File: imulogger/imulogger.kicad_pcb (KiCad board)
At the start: 2 copper layers, 64 x 25 mm, 23 parts, among them J1 DEBUG, J2 BATCONN, J3 CHGCONN, J4 Micro_SD_Card, SW1 SW_SPDT, U1 ESP32-WROOM-32, U2 USFS, U3 MCP1826S

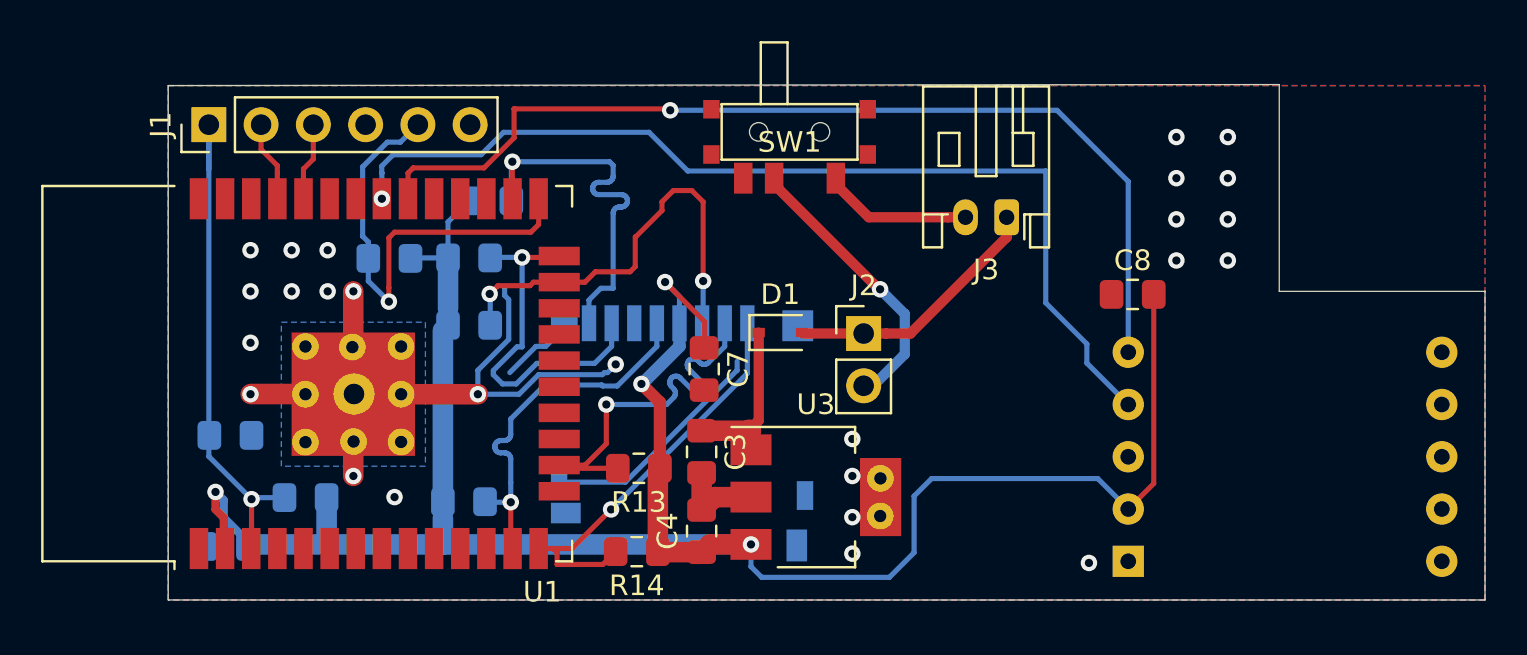
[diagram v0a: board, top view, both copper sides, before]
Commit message: make switch route V_BAT instead of GND
even though it shouldn't make a difference it's probably better to
not connect the system load to the charger.
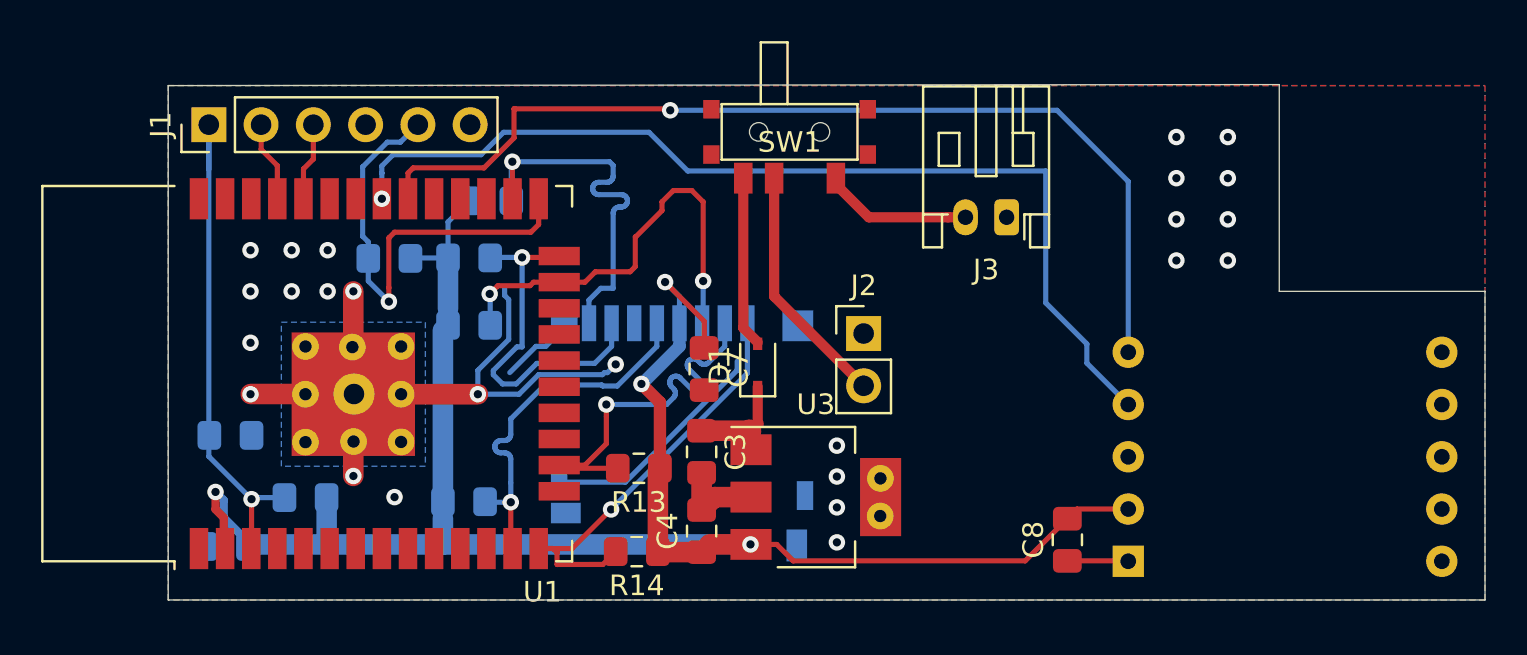
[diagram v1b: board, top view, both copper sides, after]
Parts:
- moved C8 12.3 mm to (163.7, 81.1), turned to 90 degrees
- moved D1 1.94 mm to (148.7, 72.6), turned to 90 degrees
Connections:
- J2 pad 1: Net-(D1-Pad2) -> GND
- J3 pad 1: Net-(D1-Pad2) -> GND
- SW1 pad 3: GND -> Net-(D1-Pad2)
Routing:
- net +3V3: track 110.4 -> 95.3 mm
- net Net-(D1-Pad2): track 12.9 -> 8.34 mm
- net GND: track 56.0 -> 59.0 mm, vias 26 -> 25
- net V_BAT: track 9.04 -> 6.45 mm
- net Net-(J2-Pad2): track 13.8 -> 12.7 mm, vias 1 -> 0

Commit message: optimize ground connection
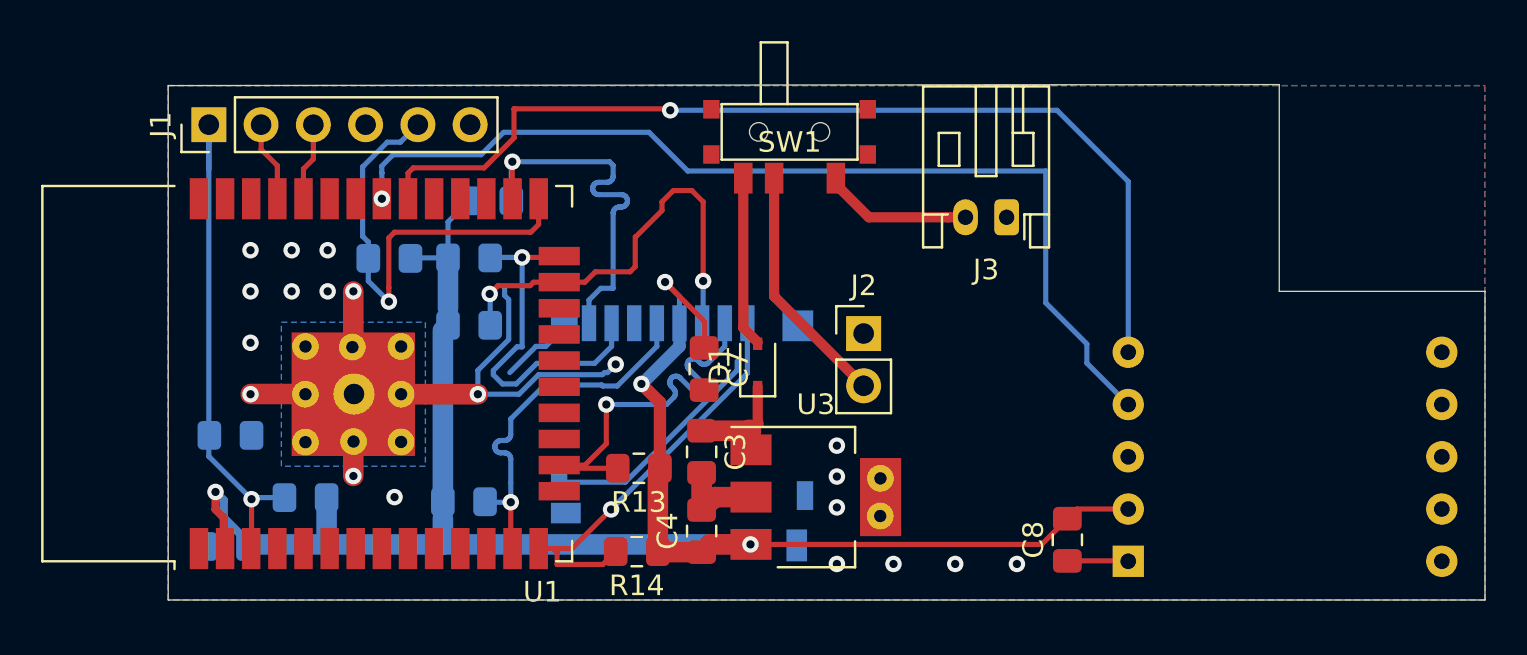
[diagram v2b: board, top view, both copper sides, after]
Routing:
- net +3V3: track 95.3 -> 94.7 mm
- net GND: vias 25 -> 20
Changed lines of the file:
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@@
     (thickness 1.6)
     (drawings 14)
-    (tracks 416)
+    (tracks 409)
     (zones 0)
     (modules 23)
@@
   (segment (start 164.17 79.58) (end 163.7 80.05) (width 0.25) (layer F.Cu) (net 1))
   (segment (start 166.66 79.58) (end 164.17 79.58) (width 0.25) (layer F.Cu) (net 1))
-  (segment (start 149.575 81.3) (end 150.375 82.1) (width 0.25) (layer F.Cu) (net 1))
-  (segment (start 148.325 81.3) (end 149.575 81.3) (width 0.25) (layer F.Cu) (net 1))
-  (segment (start 161.65 82.1) (end 163.7 80.05) (width 0.25) (layer F.Cu) (net 1))
-  (segment (start 150.375 82.1) (end 161.65 82.1) (width 0.25) (layer F.Cu) (net 1))
   (segment (start 148.3 81.3) (end 133.35 81.3) (width 1) (layer B.Cu) (net 1))
   (via (at 148.3 81.3) (size 0.8) (drill 0.4) (layers F.Cu B.Cu) (net 1))
-  (via (at 169 61.5) (size 0.8) (drill 0.4) (layers F.Cu B.Cu) (net 2))
-  (via (at 152.5 81.2) (size 0.8) (drill 0.4) (layers F.Cu B.Cu) (net 2))
+  (segment (start 162.45 81.3) (end 163.7 80.05) (width 0.25) (layer F.Cu) (net 1))
+  (segment (start 148.325 81.3) (end 162.45 81.3) (width 0.25) (layer F.Cu) (net 1))
+  (via (at 152.5 82.25) (size 0.8) (drill 0.4) (layers F.Cu B.Cu) (net 2))
   (via (at 152.5 79.5) (size 0.8) (drill 0.4) (layers F.Cu B.Cu) (net 2))
   (via (at 152.5 78) (size 0.8) (drill 0.4) (layers F.Cu B.Cu) (net 2))
@@
   (segment (start 128.995 69.005) (end 129 69) (width 0.25) (layer F.Cu) (net 2))
   (segment (start 128.995 74) (end 128.995 69.005) (width 1) (layer F.Cu) (net 2) (status 10))
-  (via (at 171.5 61.5) (size 0.8) (drill 0.4) (layers F.Cu B.Cu) (net 2))
-  (via (at 171.5 63.5) (size 0.8) (drill 0.4) (layers F.Cu B.Cu) (net 2))
-  (via (at 171.5 65.5) (size 0.8) (drill 0.4) (layers F.Cu B.Cu) (net 2))
-  (via (at 169 65.5) (size 0.8) (drill 0.4) (layers F.Cu B.Cu) (net 2))
-  (via (at 169 67.5) (size 0.8) (drill 0.4) (layers F.Cu B.Cu) (net 2))
-  (via (at 171.5 67.5) (size 0.8) (drill 0.4) (layers F.Cu B.Cu) (net 2))
-  (via (at 169 63.5) (size 0.8) (drill 0.4) (layers F.Cu B.Cu) (net 2))
   (segment (start 166.64 82.1) (end 166.66 82.12) (width 0.25) (layer F.Cu) (net 2))
   (segment (start 163.7 82.1) (end 166.64 82.1) (width 0.25) (layer F.Cu) (net 2))
+  (via (at 155.25 82.25) (size 0.8) (drill 0.4) (layers F.Cu B.Cu) (net 2))
+  (via (at 158.25 82.25) (size 0.8) (drill 0.4) (layers F.Cu B.Cu) (net 2))
+  (via (at 161.25 82.25) (size 0.8) (drill 0.4) (layers F.Cu B.Cu) (net 2))
   (via (at 124.05 79.1) (size 0.8) (drill 0.4) (layers F.Cu B.Cu) (net 3))
   (segment (start 125.65 79.025) (end 124.125 79.025) (width 0.25) (layer B.Cu) (net 3) (status 10))

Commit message: properly separate i2c and sd using ground plane
unfortunately I had to remove the 3V3 pin to achieve this
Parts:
- J1: footprint Connector_PinHeader_2.54mm:PinHeader_1x06_P2.54mm_Vertical -> Connector_PinHeader_2.54mm:PinHeader_1x05_P2.54mm_Vertical
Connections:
- J1 pad 4: (no net) -> IO0
- J1 pad 5: IO0 -> GND
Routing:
- net IO0: track 23.1 -> 21.7 mm
